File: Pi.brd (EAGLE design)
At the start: 160 x 100 mm, 9 parts, among them X1 RASPI_GPIO_B+#_BOX, X2 HDD, 5V 700mA

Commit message: Pi und Stromversorgung Rev. 2019
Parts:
- removed SV1: PLATINENVERBINDER-31SMD, homepi:PLATINENVERBINDER-31-SMD
- added JP2: (no value), pinhead:1X01
- added X3: MAC64L, con-vg:MAC64L
- moved X1 10.2 mm to (31.8, 40.6)
- moved JP1 8.98 mm to (31.8, 7.62), turned to 270 degrees
- moved R1 6.48 mm to (149.9, 15.2)
- moved R2 6.48 mm to (146.1, 6.35)
- moved LED1 6.48 mm to (153.7, 17.8)
- moved LED2 6.48 mm to (153.7, 7.62)
- moved RPI1 4.58 mm to (55.9, 30.5)
- moved X2 4.02 mm to (29.2, 88.9)
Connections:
- new net +24V: X3.A32, X3.C32
- new net +5V_EXT: X3.A31, X3.C31
- new net GND_EXT: X3.A30, X3.C30
- new net PI_RESET: JP2.1, X3.C7
- new net RXD: X1.10, X3.C27
- new net TXD: X1.8, X3.C26
- net +3,3V: now also X3.A2, X3.C2; no longer SV1.2, SV1.2T
- net +5V_INT: now also X3.A1, X3.C1; no longer SV1.1, SV1.1T
- net +5V_INT2: now also X3.A28, X3.C28; no longer SV1.28, SV1.28T
- net 1WIRE: now also X3.A7; no longer SV1.7, SV1.7T
- net GND_INT: now also X3.A29, X3.A3, X3.A6, X3.A8, X3.C29, X3.C3, X3.C6, X3.C8; no longer SV1.29, SV1.29T, SV1.3, SV1.3T, SV1.6, SV1.6T, SV1.8, SV1.8T
- net GPIO.05: now also X3.A14; no longer SV1.14, SV1.14T
- net GPIO.06: now also X3.A15; no longer SV1.15, SV1.15T
- net GPIO.12: now also X3.A16; no longer SV1.16, SV1.16T
- net GPIO.13: now also X3.A17; no longer SV1.17, SV1.17T
- net GPIO.16: now also X3.A18; no longer SV1.18, SV1.18T
- net GPIO.17: now also X3.A19; no longer SV1.19, SV1.19T
- net GPIO.18: now also X3.A20; no longer SV1.20, SV1.20T
- net GPIO.19: now also X3.A21; no longer SV1.21, SV1.21T
- net GPIO.20: now also X3.A22; no longer SV1.22, SV1.22T
- net GPIO.21: now also X3.A23; no longer SV1.23, SV1.23T
- net GPIO.22: now also X3.A24; no longer SV1.24, SV1.24T
- net GPIO.23: now also X3.A25; no longer SV1.25, SV1.25T
- net GPIO.24: now also X3.A26; no longer SV1.26, SV1.26T
- net GPIO.25: now also X3.A27; no longer SV1.27, SV1.27T
- net I2C_SCL: now also X3.A5; no longer SV1.5, SV1.5T
- net I2C_SDA: now also X3.A4; no longer SV1.4, SV1.4T
- net SPI_CE0: now also X3.A12; no longer SV1.12, SV1.12T
- net SPI_CE1: now also X3.A13; no longer SV1.13, SV1.13T
- net SPI_MISO: now also X3.A10; no longer SV1.10, SV1.10T
- net SPI_MOSI: now also X3.A9; no longer SV1.9, SV1.9T
- net SPI_SCLK: now also X3.A11; no longer SV1.11, SV1.11T
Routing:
- net PI_RESET: track 0.00 -> 94.1 mm
- net TXD: track 0.00 -> 67.8 mm, vias 0 -> 1
- net RXD: track 0.00 -> 67.8 mm, vias 0 -> 1
- net GPIO.24: track 50.3 -> 63.8 mm, vias 1 -> 2
- net GPIO.23: track 50.3 -> 63.7 mm, vias 1 -> 2
- net GPIO.22: track 52.8 -> 65.6 mm, vias 1 -> 2
- net GPIO.25: track 50.0 -> 62.0 mm, vias 1 -> 2
- net GPIO.18: track 42.7 -> 54.6 mm, vias 1 -> 2
- net SPI_SCLK: track 42.7 -> 31.4 mm
- net GPIO.13: track 42.7 -> 31.4 mm
- net GPIO.06: track 42.7 -> 31.4 mm
- net GPIO.05: track 42.7 -> 31.4 mm
- net SPI_CE1: track 39.1 -> 27.8 mm
- net SPI_CE0: track 39.1 -> 27.8 mm
- net GPIO.12: track 39.1 -> 27.8 mm
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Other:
- board text added: "HomePi Hauptplatine Rev 2019/03 (c) Peter Müller"
- board text removed: "HomePi Hauptplatine Rev 2015/12 (c) Peter Müller"

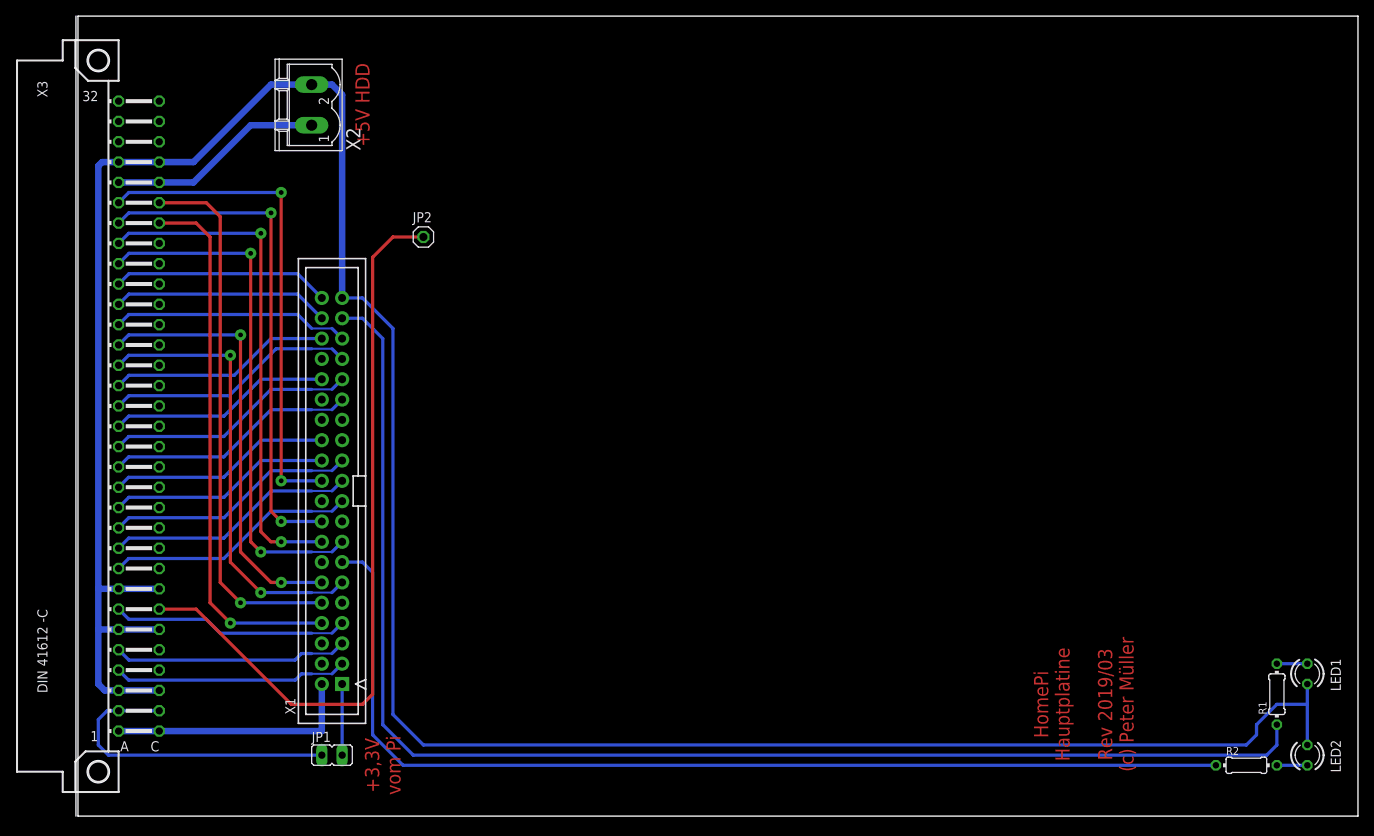
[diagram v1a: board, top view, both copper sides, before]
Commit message: Anpassungen an Rev. 2019, erste Can-Bus Elemente
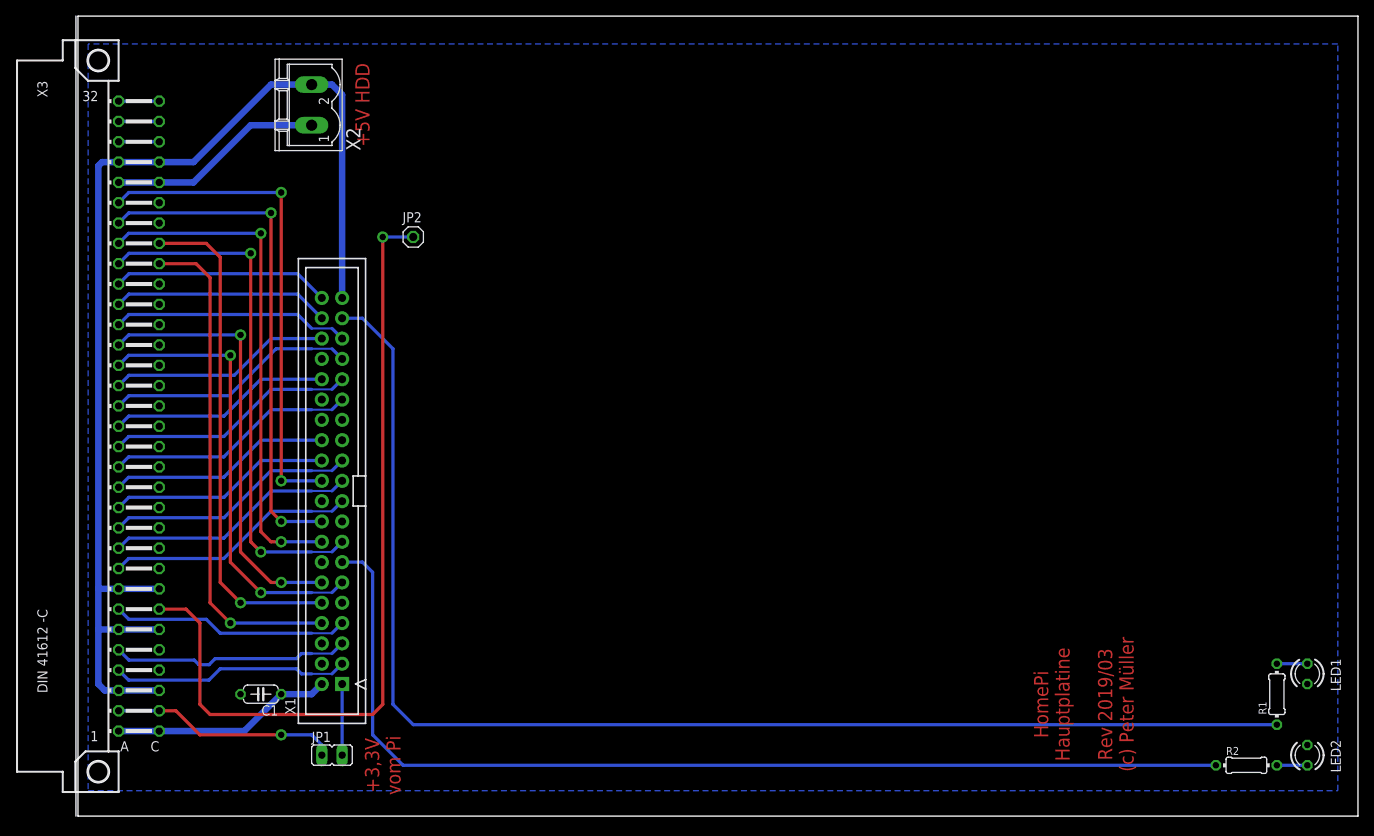
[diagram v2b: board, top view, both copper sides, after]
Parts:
- added C1: (no value), rcl:C050-024X044
- moved JP2 1.27 mm to (41.9, 72.4)
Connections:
- removed net GND_A: X1.6
- removed net GND_B: X1.9
- removed net GND_C: X1.14
- removed net GND_D: X1.20
- removed net GND_E: X1.25
- removed net GND_F: X1.30
- removed net GND_G: X1.34
- removed net GND_INT: LED1.K, LED2.K, X1.39, X2.2, X3.A29, X3.A3, X3.A6, X3.A8, X3.C29, X3.C3, X3.C6, X3.C8
- new net GND: C1.2, LED1.K, LED2.K, X1.14, X1.20, X1.25, X1.30, X1.34, X1.39, X1.6, X1.9, X2.2, X3.A29, X3.A3, X3.A6, X3.A8, X3.C29, X3.C3, X3.C6, X3.C8
- new net RS485_A: X3.C26
- new net RS495_B: X3.C27
- net +5V_INT: now also C1.1
- net RXD: now also X3.C25; no longer X3.C27
- net TXD: now also X3.C24; no longer X3.C26
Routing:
- net GND_INT: track 331.1 -> 0.00 mm
- net GND: track 0.00 -> 148.6 mm
- net +3,3V: track 39.7 -> 28.4 mm, vias 0 -> 1
- net PI_RESET: track 94.1 -> 102.1 mm, vias 0 -> 1
- net GPIO.26: track 170.8 -> 163.9 mm
- net TXD: track 67.8 -> 62.7 mm
- net RXD: track 67.8 -> 62.7 mm
- net GND_EXT: track 0.00 -> 5.08 mm
- net +5V_EXT: track 0.00 -> 5.08 mm
- net +24V: track 0.00 -> 5.08 mm
- net +5V_INT: track 31.3 -> 27.8 mm
- net I2C_SDA: track 29.3 -> 29.8 mm
- added copper zone on layer 16, net GND

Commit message: Can-Bus, Reset für den RasPi, Kleinere Optimierungen
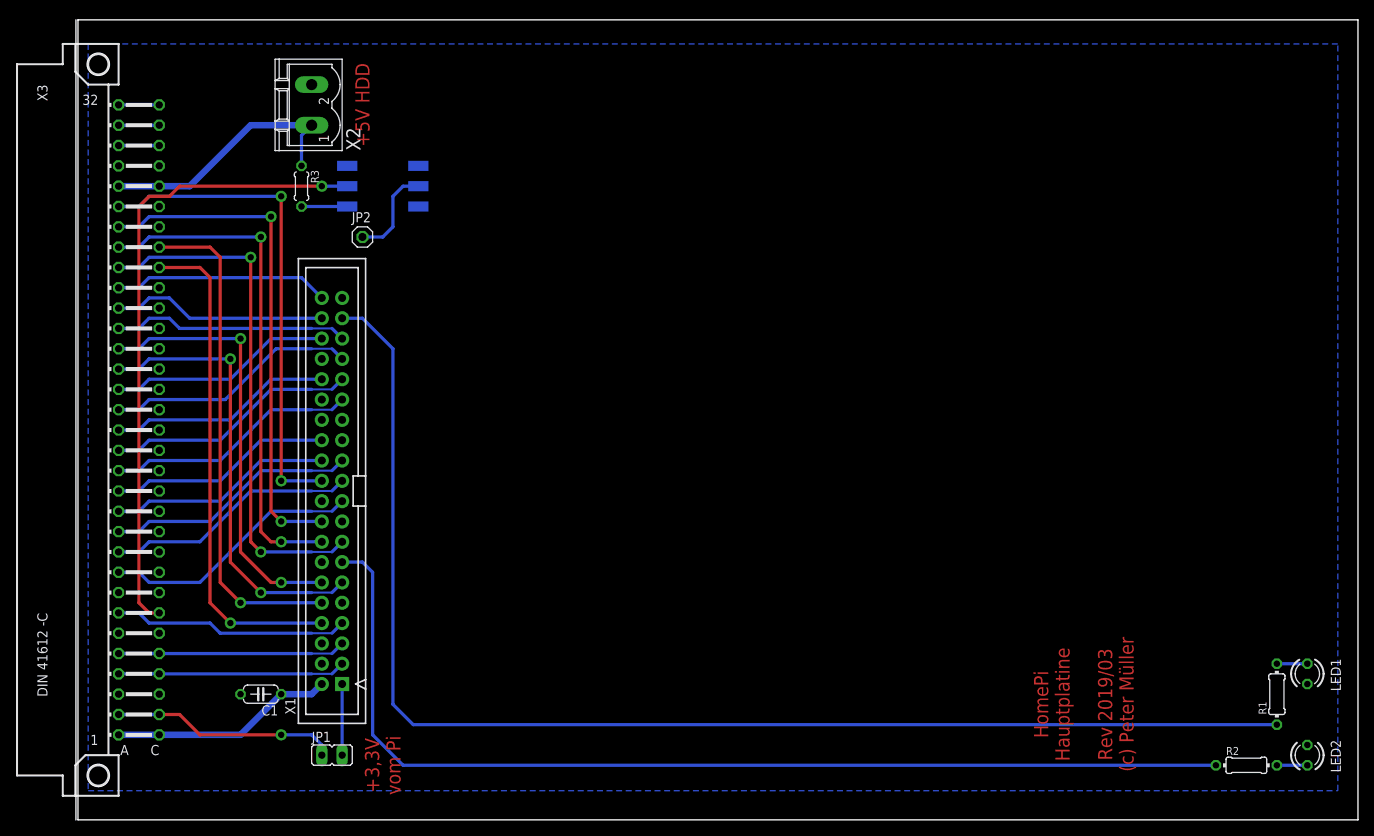
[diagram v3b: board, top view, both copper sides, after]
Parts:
- added OK1: CNY17SMD, homepi:DIL06_SMD
- added R3: 330R, rcl:0204/5
- R1, R2: value 560 -> 560R
- moved JP2 6.35 mm to (35.6, 72.4)
- moved X3 0.47 mm to (2.54, 49.5)
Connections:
- removed net PI_RESET: JP2.1, X3.C7
- new net !PI_RESET: OK1.2, X3.C7
- new net N$2: OK1.1, R3.2
- new net N$3: JP2.1, OK1.5
- net +5V_INT2: now also R3.1
- net GND: now also OK1.4
- net I2C_SCL: now also X3.C5
- net I2C_SDA: now also X3.C4
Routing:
- net GND: track 148.6 -> 0.00 mm
- net PI_RESET: track 102.1 -> 0.00 mm, vias 1 -> 0
- net !PI_RESET: track 0.00 -> 79.7 mm, vias 0 -> 1
- net N$3: track 0.00 -> 11.8 mm
- net +5V_INT2: track 27.1 -> 32.9 mm
- net N$2: track 0.00 -> 5.71 mm
- net I2C_SDA: track 29.8 -> 28.5 mm
- net I2C_SCL: track 29.8 -> 28.5 mm
- net SPI_MOSI: track 31.4 -> 32.7 mm
- net GPIO.22: track 65.6 -> 65.1 mm

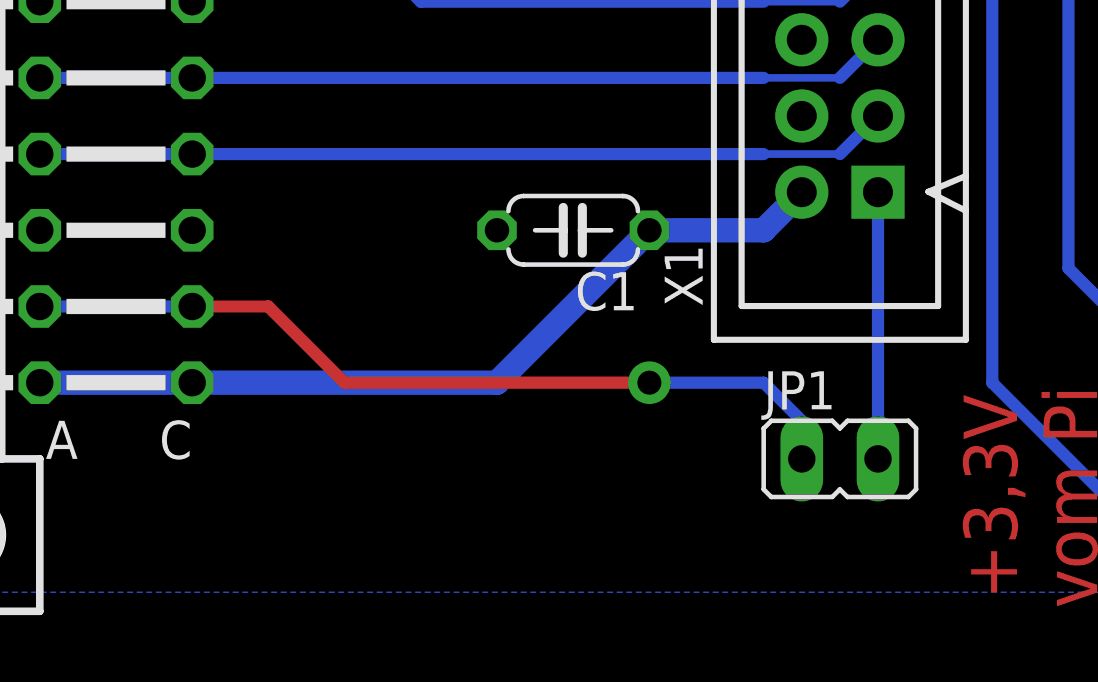
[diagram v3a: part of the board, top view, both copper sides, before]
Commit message: 3,3V-Versorgung nur noch über TSR-Spannungsregler
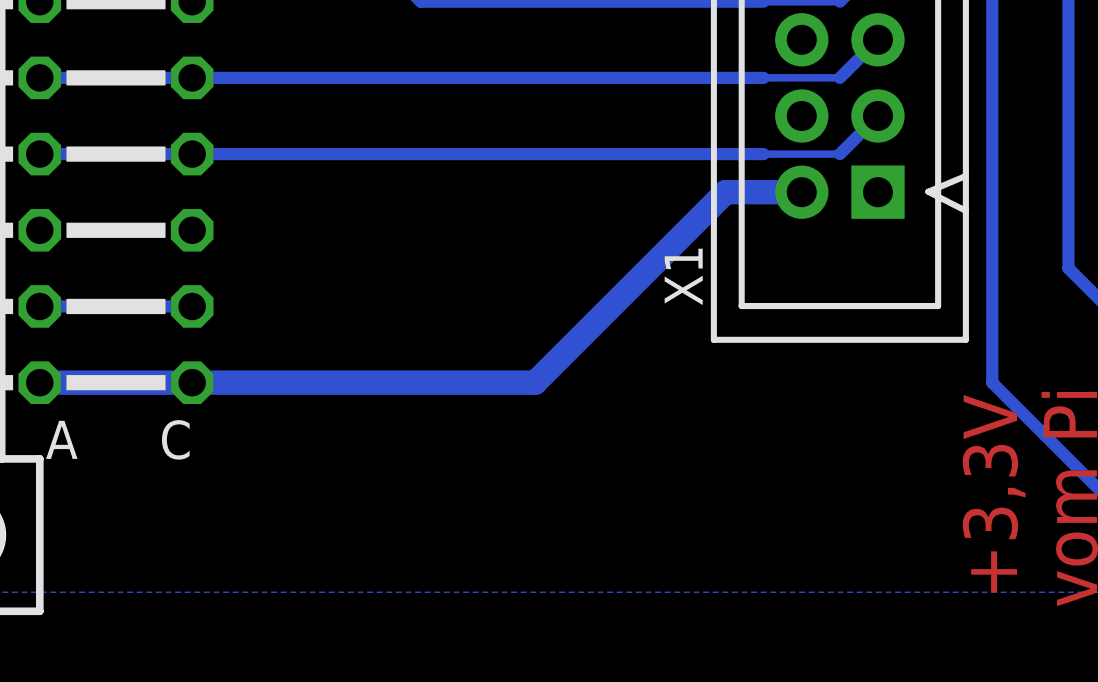
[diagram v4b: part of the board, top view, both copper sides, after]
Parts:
- removed C1: (no value), rcl:C050-024X044
- removed JP1: (no value), jumper:JP1
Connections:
- removed net N$9: JP1.2, X1.1
- new net 3V3A: X1.1
- net +3,3V: no longer JP1.1
- net +5V_INT: no longer C1.1
- net GND: no longer C1.2
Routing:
- net +3,3V: track 28.2 -> 5.08 mm, vias 1 -> 0
- net N$9: track 8.89 -> 0.00 mm
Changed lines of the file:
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@@
 <element name="X1" library="raspberrypi_bastelstube_v13" package="RASPI_GPIO_B+_BOX" value="RASPI_GPIO_B+#_BOX" x="31.75" y="40.64" rot="R90"/>
 <element name="RPI1" library="homepi" package="RASPBERRYPI-PLATINE" value="RASPBERRYPI-PLATINE" x="55.88" y="30.48"/>
-<element name="JP1" library="jumper" package="JP1" value="" x="31.75" y="7.62" rot="R270"/>
 <element name="R1" library="rcl" package="0204/7" value="560R" x="149.86" y="15.24" rot="R90"/>
 <element name="LED1" library="led" package="LED3MM" value="gn 2mA" x="153.67" y="17.78" smashed="yes" rot="R270">
@@
 <element name="X3" library="con-vg" package="MAC64L" value="MAC64L" x="2.54" y="49.53" rot="R180"/>
 <element name="JP2" library="pinhead" package="1X01" value="" x="35.56" y="72.39"/>
-<element name="C1" library="rcl" package="C050-024X044" value="" x="22.86" y="15.24" rot="R180"/>
 <element name="OK1" library="homepi" package="DIL06_SMD" value="CNY17SMD" x="38.1" y="78.74" rot="MR90"/>
 <element name="R3" library="rcl" package="0204/5" value="330R" x="27.94" y="78.74" rot="R270"/>
@@
 <wire x1="40.64" y1="6.35" x2="142.24" y2="6.35" width="0.4064" layer="16"/>
 </signal>
-<signal name="N$9">
-<contactref element="X1" pad="1"/>
-<contactref element="JP1" pad="2"/>
-<wire x1="33.02" y1="16.51" x2="33.02" y2="7.62" width="0.4064" layer="16"/>
-</signal>
 <signal name="+3,3V">
-<contactref element="JP1" pad="1"/>
 <contactref element="X3" pad="A2"/>
 <contactref element="X3" pad="C2"/>
 <wire x1="10.16" y1="12.7" x2="5.08" y2="12.7" width="0.4064" layer="16"/>
-<via x="25.4" y="10.16" extent="1-16" drill="0.8" diameter="1.4224"/>
-<wire x1="25.4" y1="10.16" x2="29.21" y2="10.16" width="0.4064" layer="16"/>
-<wire x1="29.21" y1="10.16" x2="30.48" y2="8.89" width="0.4064" layer="16"/>
-<wire x1="30.48" y1="8.89" x2="30.48" y2="7.62" width="0.4064" layer="16"/>
-<wire x1="25.4" y1="10.16" x2="15.24" y2="10.16" width="0.4064" layer="1"/>
-<wire x1="10.16" y1="12.7" x2="12.7" y2="12.7" width="0.4064" layer="1"/>
-<wire x1="12.7" y1="12.7" x2="15.24" y2="10.16" width="0.4064" layer="1"/>
 </signal>
 <signal name="N$15">
@@
 <contactref element="X3" pad="C1"/>
 <wire x1="10.16" y1="10.16" x2="5.08" y2="10.16" width="0.8128" layer="16"/>
-<contactref element="C1" pad="1"/>
-<wire x1="30.48" y1="16.51" x2="29.21" y2="15.24" width="0.8128" layer="16"/>
-<wire x1="29.21" y1="15.24" x2="25.4" y2="15.24" width="0.8128" layer="16"/>
-<wire x1="25.4" y1="15.24" x2="20.32" y2="10.16" width="0.8128" layer="16"/>
-<wire x1="10.16" y1="10.16" x2="20.32" y2="10.16" width="0.8128" layer="16"/>
+<wire x1="10.16" y1="10.16" x2="21.59" y2="10.16" width="0.8128" layer="16"/>
+<wire x1="30.48" y1="16.51" x2="27.94" y2="16.51" width="0.8128" layer="16"/>
+<wire x1="27.94" y1="16.51" x2="21.59" y2="10.16" width="0.8128" layer="16"/>
 </signal>
 <signal name="GND_EXT">
@@
 </signal>
 <signal name="GND">
-<contactref element="C1" pad="2"/>
 <contactref element="X2" pad="2"/>
 <contactref element="X1" pad="39"/>
@@
 <wire x1="30.48" y1="78.74" x2="33.655" y2="78.74" width="0.4064" layer="16"/>
 </signal>
+<signal name="3V3A">
+<contactref element="X1" pad="1"/>
+</signal>
 </signals>
